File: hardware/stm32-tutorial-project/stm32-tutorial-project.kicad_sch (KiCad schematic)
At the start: 47 parts, among them J2 10pin IDC SWD, J3 Conn_01x04, J4 Conn_01x04, J5 Conn_01x13, J6 Conn_01x13, Q1 NPN, Q3 PNP, SW1 SW_Push, SW2 SW_Push_SPDT, U1 STM32G431CBTx

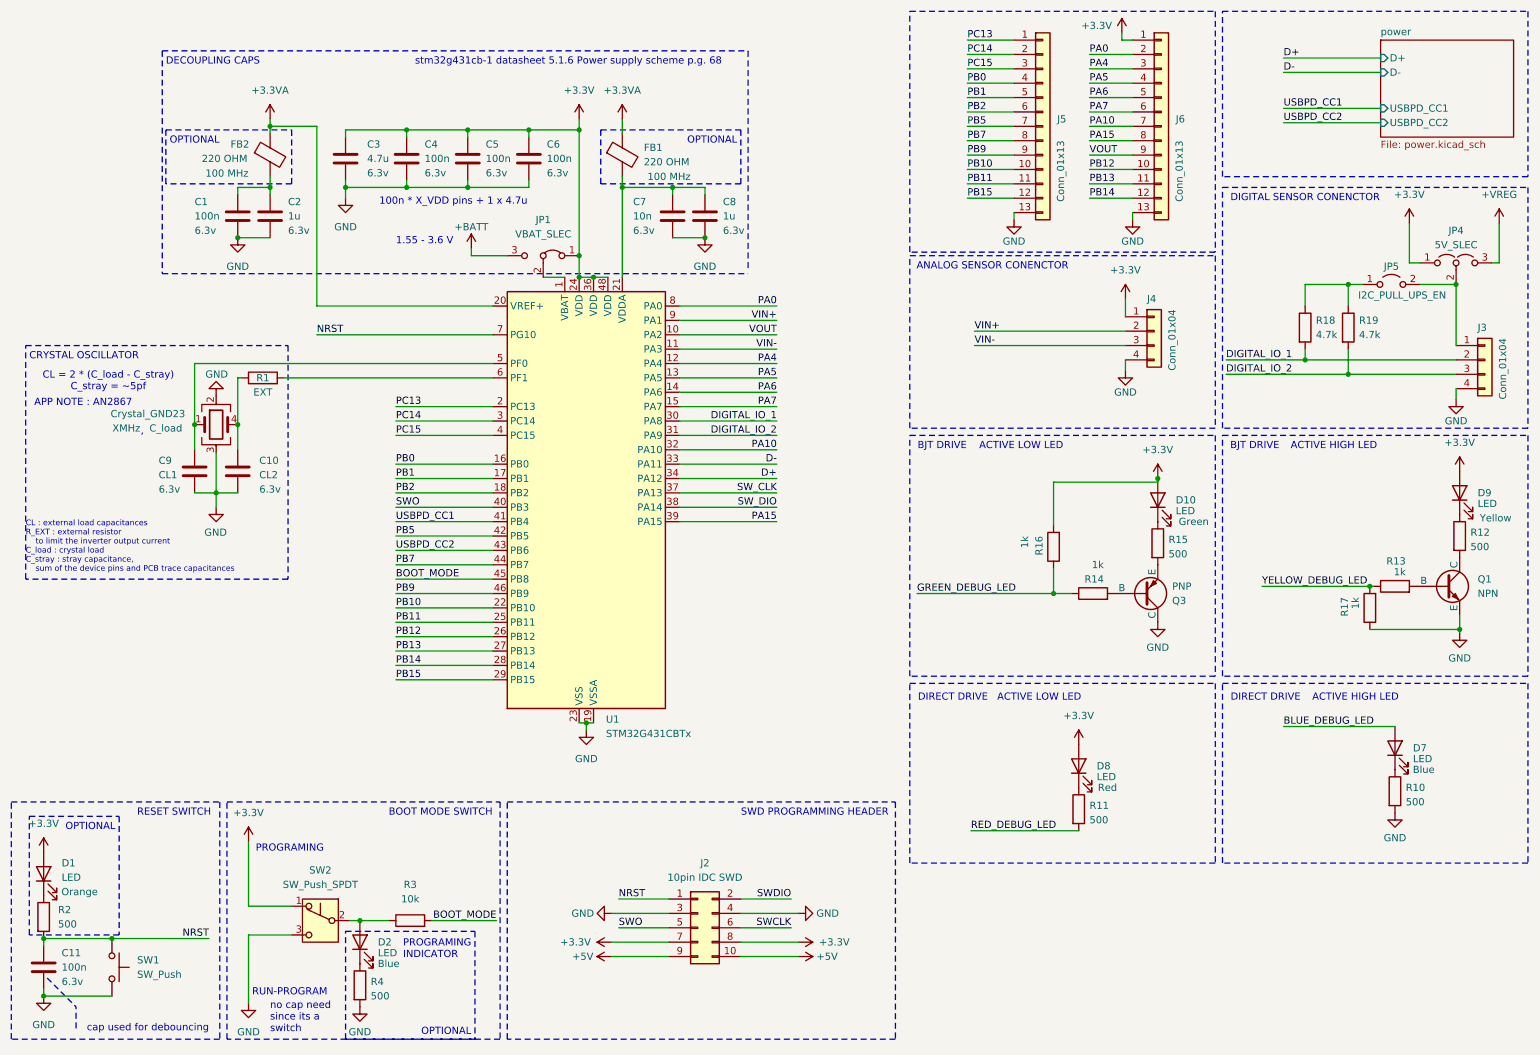
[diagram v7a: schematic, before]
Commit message: fixed leds and added debug leds to stm32 pins oops
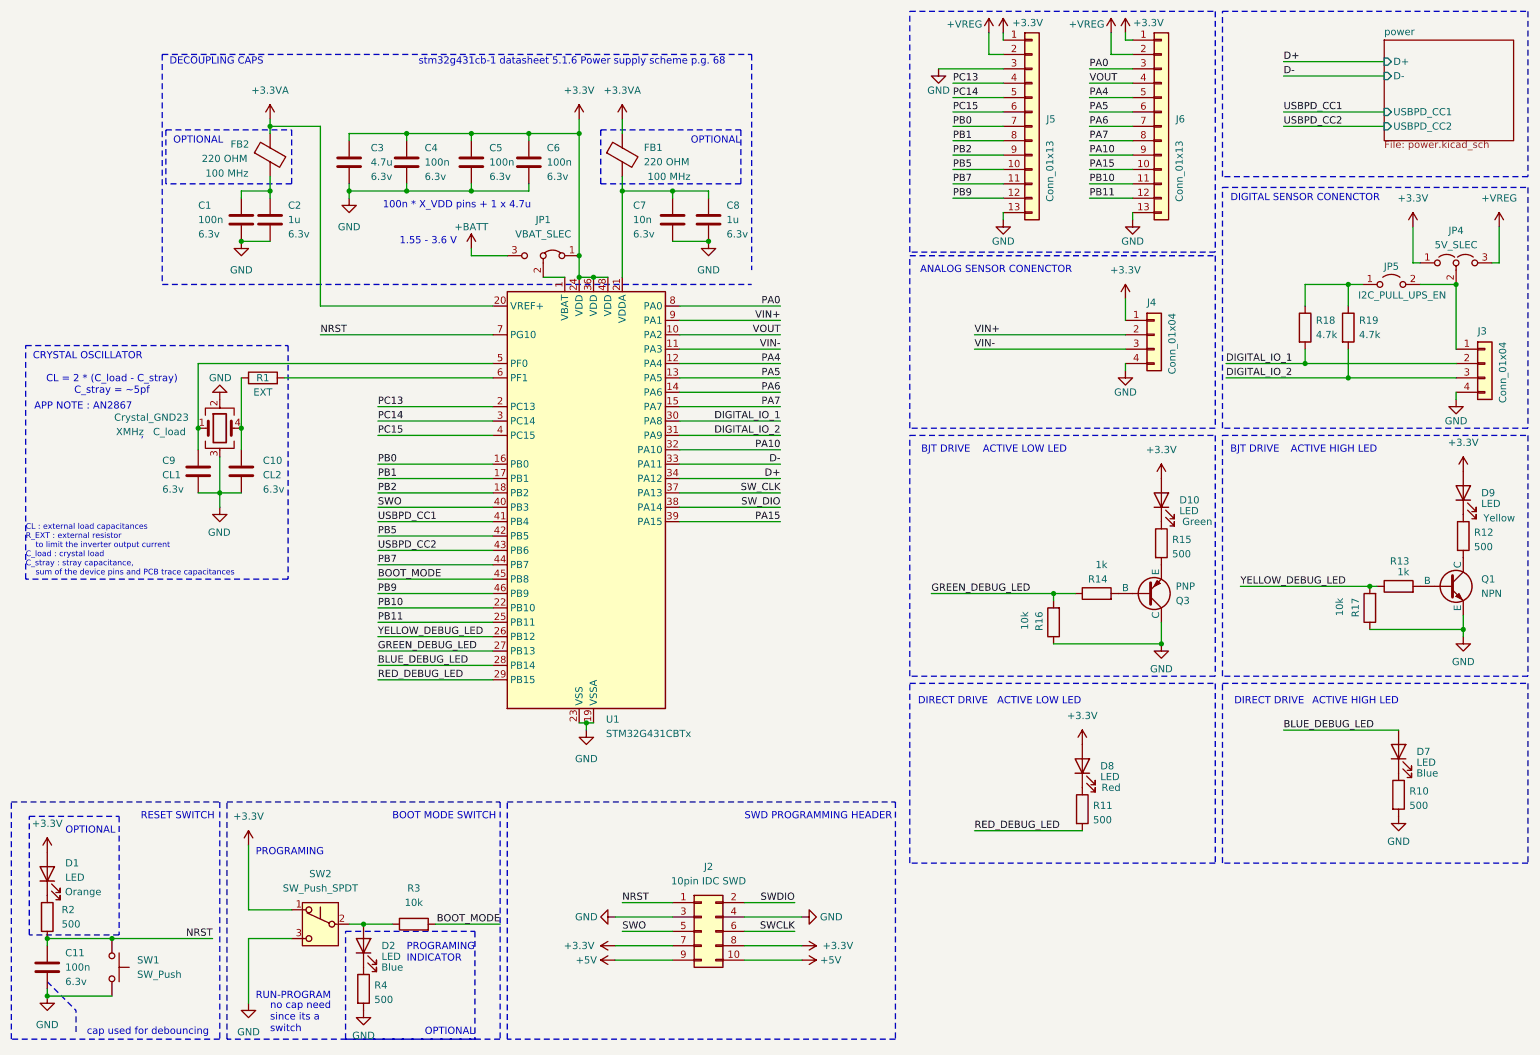
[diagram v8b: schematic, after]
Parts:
- R16, R17: value 1k -> 10k
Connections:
- net +3.3V: now also J5.1 (Pin_1); no longer R16.2
- net +VREG: now also J5.2 (Pin_2), J6.2 (Pin_2)
- net BLUE_DEBUG_LED: now also U1.28 (PB14)
- net GND: now also J5.3 (Pin_3), R16.1
- net GREEN_DEBUG_LED: now also R16.2, U1.27 (PB13); no longer R16.1
- net PA0: now also J6.3 (Pin_3); no longer J6.2 (Pin_2)
- net PA10: now also J6.9 (Pin_9); no longer J6.7 (Pin_7)
- net PA15: now also J6.10 (Pin_10); no longer J6.8 (Pin_8)
- net PA4: now also J6.5 (Pin_5); no longer J6.3 (Pin_3)
- net PA5: now also J6.6 (Pin_6); no longer J6.4 (Pin_4)
- net PA6: now also J6.7 (Pin_7); no longer J6.5 (Pin_5)
- net PA7: now also J6.8 (Pin_8); no longer J6.6 (Pin_6)
- net PB0: now also J5.7 (Pin_7); no longer J5.4 (Pin_4)
- net PB1: now also J5.8 (Pin_8); no longer J5.5 (Pin_5)
- net PB10: now also J6.11 (Pin_11); no longer J5.10 (Pin_10)
- net PB11: now also J6.12 (Pin_12); no longer J5.11 (Pin_11)
- net PB2: now also J5.9 (Pin_9); no longer J5.6 (Pin_6)
- net PB5: now also J5.10 (Pin_10); no longer J5.7 (Pin_7)
- net PB7: now also J5.11 (Pin_11); no longer J5.8 (Pin_8)
- net PB9: now also J5.12 (Pin_12); no longer J5.9 (Pin_9)
- net PC13: now also J5.4 (Pin_4); no longer J5.1 (Pin_1)
- net PC14: now also J5.5 (Pin_5); no longer J5.2 (Pin_2)
- net PC15: now also J5.6 (Pin_6); no longer J5.3 (Pin_3)
- net RED_DEBUG_LED: now also U1.29 (PB15)
- net VOUT: now also J6.4 (Pin_4); no longer J6.9 (Pin_9)
- net YELLOW_DEBUG_LED: now also U1.26 (PB12)
- removed net PB12: J6.10 (Pin_10), U1.26 (PB12)
- removed net PB13: J6.11 (Pin_11), U1.27 (PB13)
- removed net PB14: J6.12 (Pin_12), U1.28 (PB14)
- removed net PB15: J5.12 (Pin_12), U1.29 (PB15)
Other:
- moved on the sheet: C1, C10, C11, C2, C3, C4, C5, C6, C7, C8, C9, D1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
